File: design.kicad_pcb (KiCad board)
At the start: 2 copper layers, 80 x 55 mm, 92 parts, among them J1 2601-3108, J10 Conn_01x04, J11 Conn_01x04, J12 Conn_01x03, J13 Conn_01x03, J14 BM04B-SRSS-TB_LF__SN_, J2 2601-3108, J3 2601-3108, J4 TYPE-C-31-M-12, J5 SKEDD-UPDI-4, J6 Conn_01x04, J7 Conn_01x04, J8 Conn_01x04, J9 Conn_01x04, Q1 AO3400A, Q2 AO3400A, SW1 K3-2235S-K1, SW2 K3-2235S-K1, U1 ATtiny1616-S, U2 AP2112K-3.3, U3 CP2105, U4 ATtiny1616-M

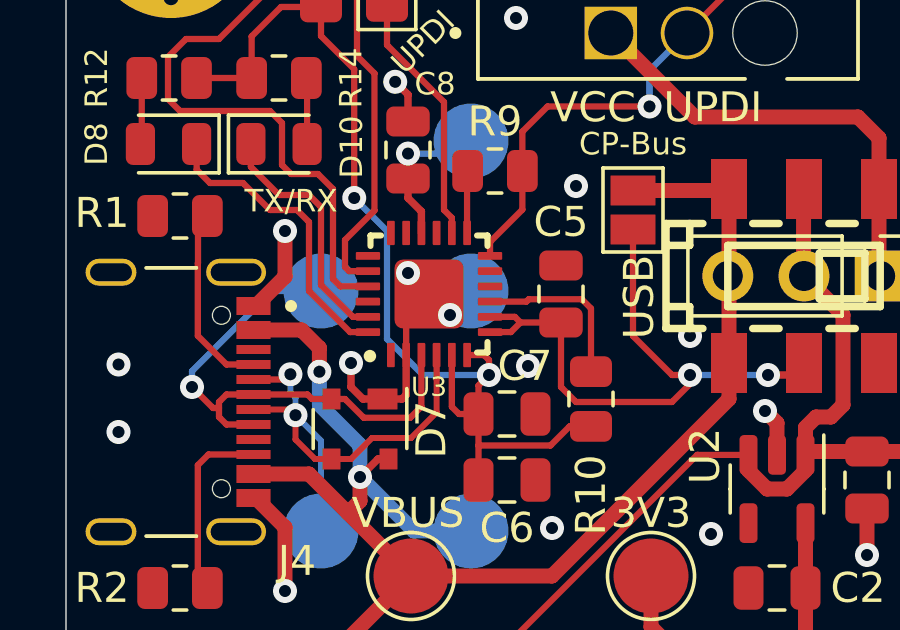
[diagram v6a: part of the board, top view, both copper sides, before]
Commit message: remove via
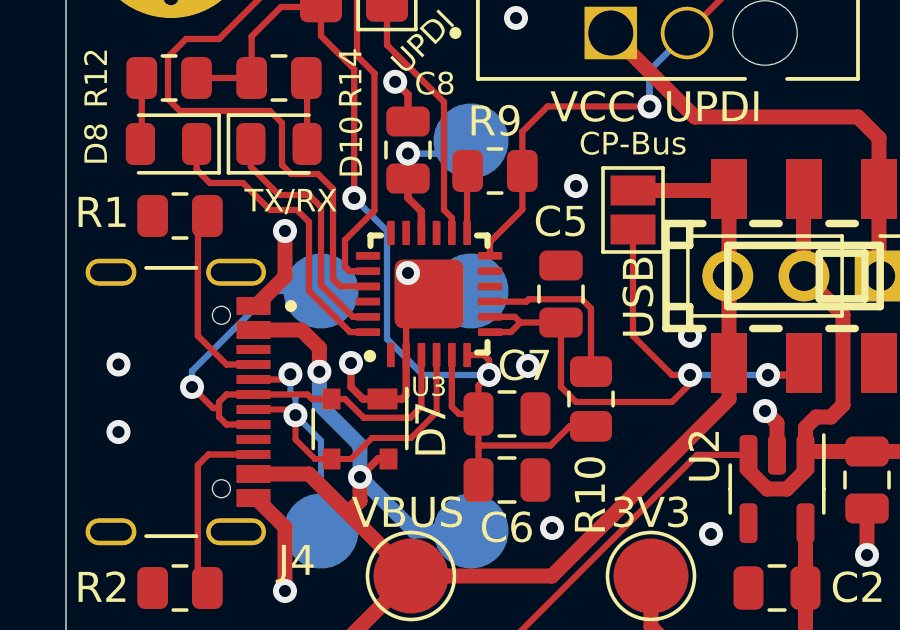
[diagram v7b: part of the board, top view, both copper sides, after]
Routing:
- net GND: vias 72 -> 71
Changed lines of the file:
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@@
   (via (at 154.2 98.1) (size 0.8) (drill 0.4) (layers "F.Cu" "B.Cu") (free) (net 28))
   (via (at 125 87.75) (size 0.8) (drill 0.4) (layers "F.Cu" "B.Cu") (free) (net 28))
-  (via (at 100.3 81.8) (size 0.8) (drill 0.4) (layers "F.Cu" "B.Cu") (net 28))
   (via (at 118.8 78.3) (size 0.8) (drill 0.4) (layers "F.Cu" "B.Cu") (free) (net 28))
   (via (at 141.6 86.2) (size 0.8) (drill 0.4) (layers "F.Cu" "B.Cu") (free) (net 28))
